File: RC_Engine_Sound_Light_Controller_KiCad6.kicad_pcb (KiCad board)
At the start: 2 copper layers, 71.5 x 39.5 mm, 39 parts, among them J1 RX, J10 RGB, J11 32, J12 CH1, J13 CH2, J14 CH3, J15 ESC, J16 CH4, J2 HeadL, J3 TailL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

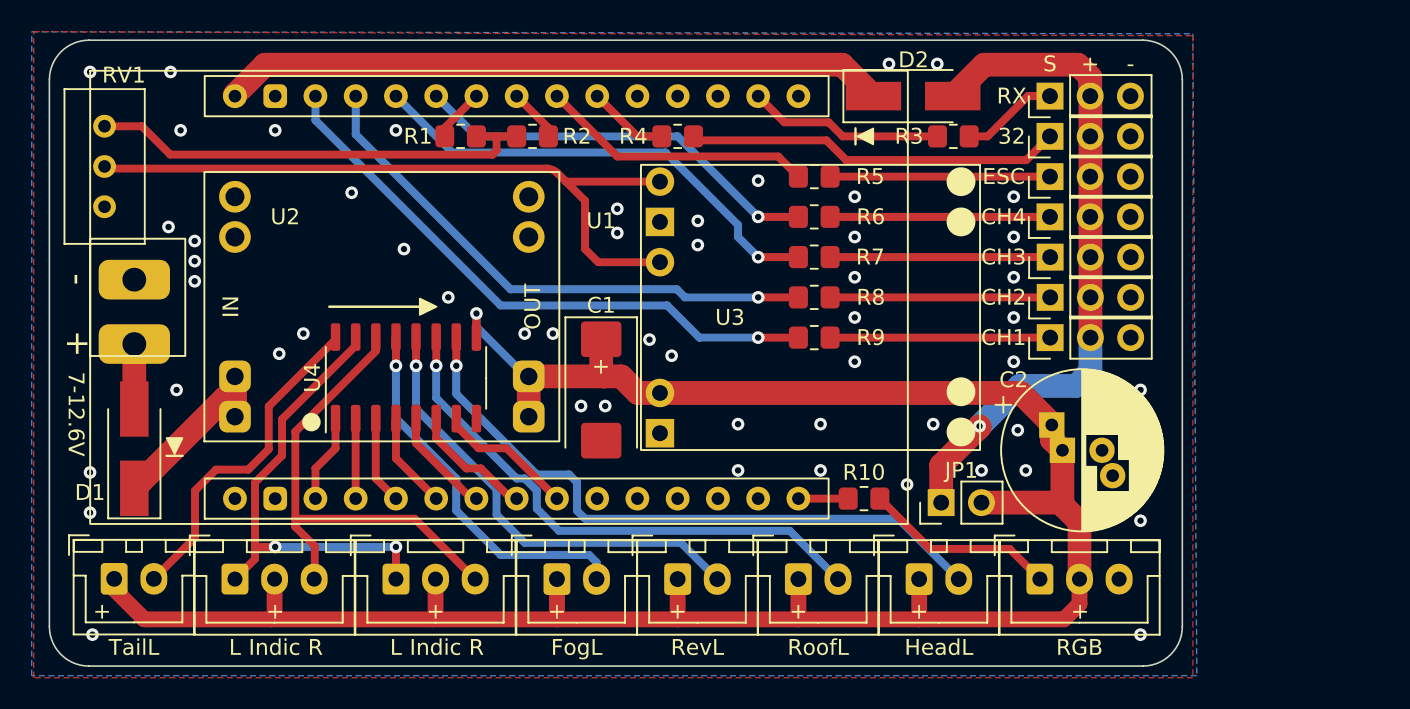
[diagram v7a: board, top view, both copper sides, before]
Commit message: Added battery voltage measurement divider, cap and (re-added) EN cap on the backside (optional).
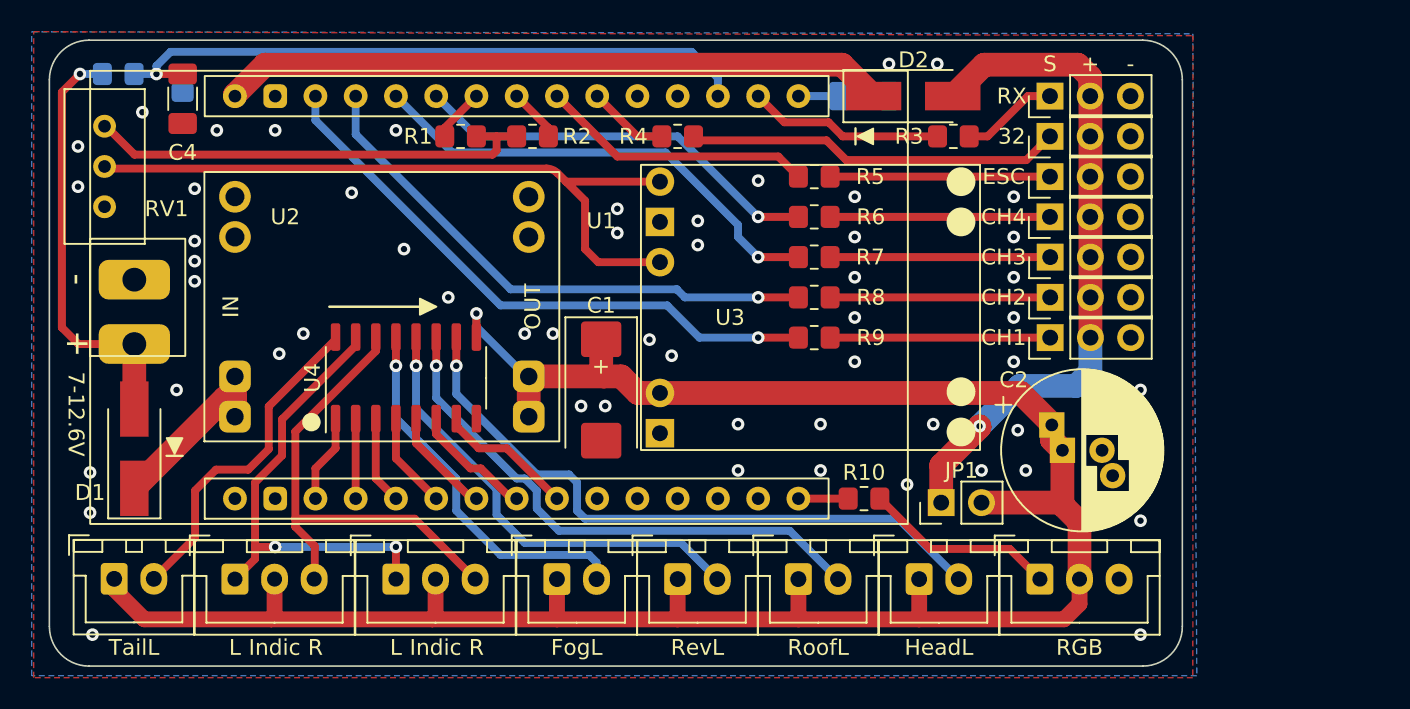
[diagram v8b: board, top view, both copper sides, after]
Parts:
- added C3: 4.7µF, Capacitor_SMD:C_1206_3216Metric_Pad1.33x1.80mm_HandSolder, B.Cu at (132.4, 49.5)
- added C4: 100nF, Capacitor_SMD:C_1206_3216Metric_Pad1.33x1.80mm_HandSolder, F.Cu at (89.4, 49.7)
- added R11: 22kΩ, Resistor_SMD:R_0805_2012Metric_Pad1.20x1.40mm_HandSolder, B.Cu at (85.3, 48.1)
- added R12: 100kΩ, Resistor_SMD:R_0805_2012Metric_Pad1.20x1.40mm_HandSolder, B.Cu at (89.4, 50.3)
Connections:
- U1 pad 16: unconnected-(U1-Pad16) -> /EN_PIN
- U1 pad 18: unconnected-(U1-Pad18) -> D39
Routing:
- net D39: track 0.00 -> 43.7 mm, vias 0 -> 1
- net +BATT: track 4.10 -> 27.0 mm, vias 0 -> 1
- net /EN_PIN: track 0.00 -> 2.59 mm
- net -BATT: vias 53 -> 54
